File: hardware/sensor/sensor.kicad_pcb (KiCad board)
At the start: 2 copper layers, 29 x 31 mm, 56 parts, among them P1 CONN_01X05, SW1 Reset, T1 BUK9Y22, U1 LMR16006, U2 OPA376AIDCK, U3 CD74HC4046, U4 CD74HC4046, U5 Atmel_SAM_D09, X1 60V, X2 UART

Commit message: Cleanup seems done
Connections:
- P1 pad : (no net) -> GND
- RV1 pad 4: (no net) -> GND
- RV2 pad 4: (no net) -> GND
- U3 pad 14: GND -> Net-(U3-Pad14)
- X2 pad : (no net) -> GND
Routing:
- net GND: track 30.5 -> 41.5 mm, vias 7 -> 9
- net Net-(U5-Pad4): track 15.2 -> 9.69 mm
- net /RX1_out: track 26.4 -> 24.6 mm, vias 3 -> 2

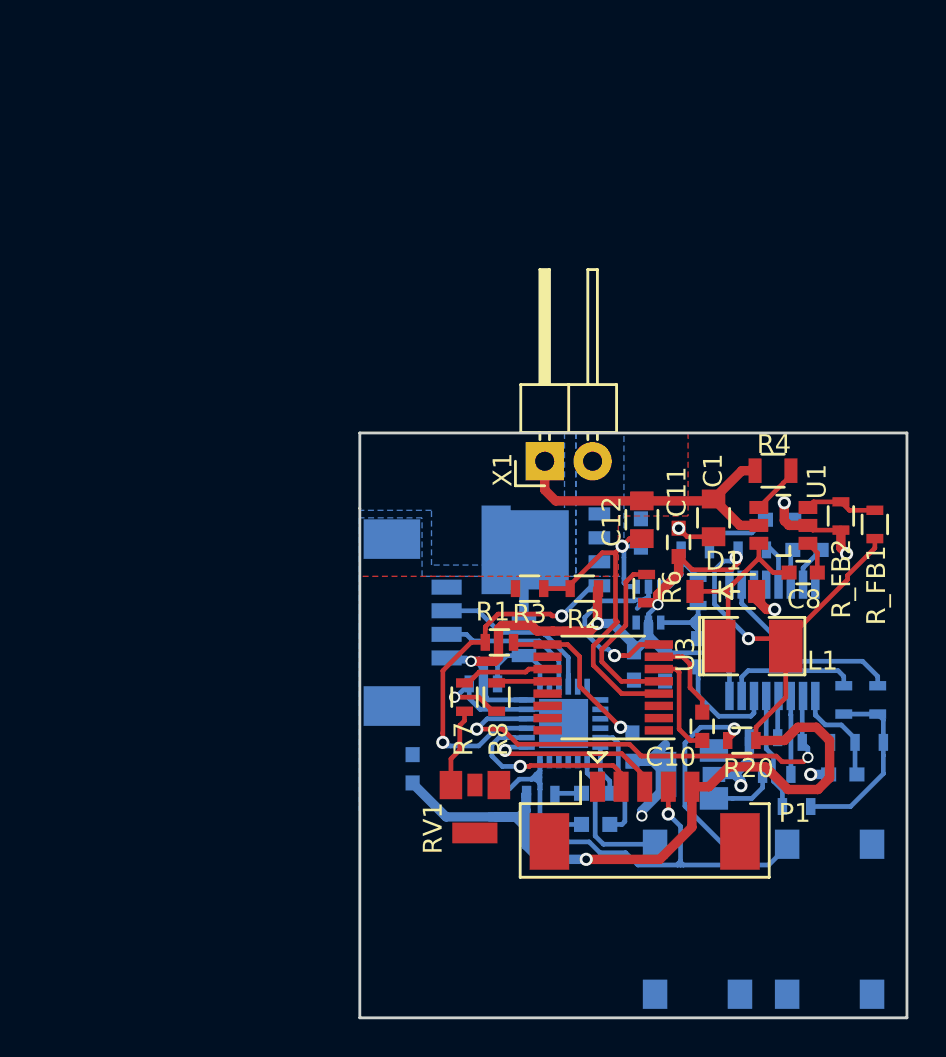
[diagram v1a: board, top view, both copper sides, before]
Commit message: Routing done with Gate Driver. Testpoints are left for now.
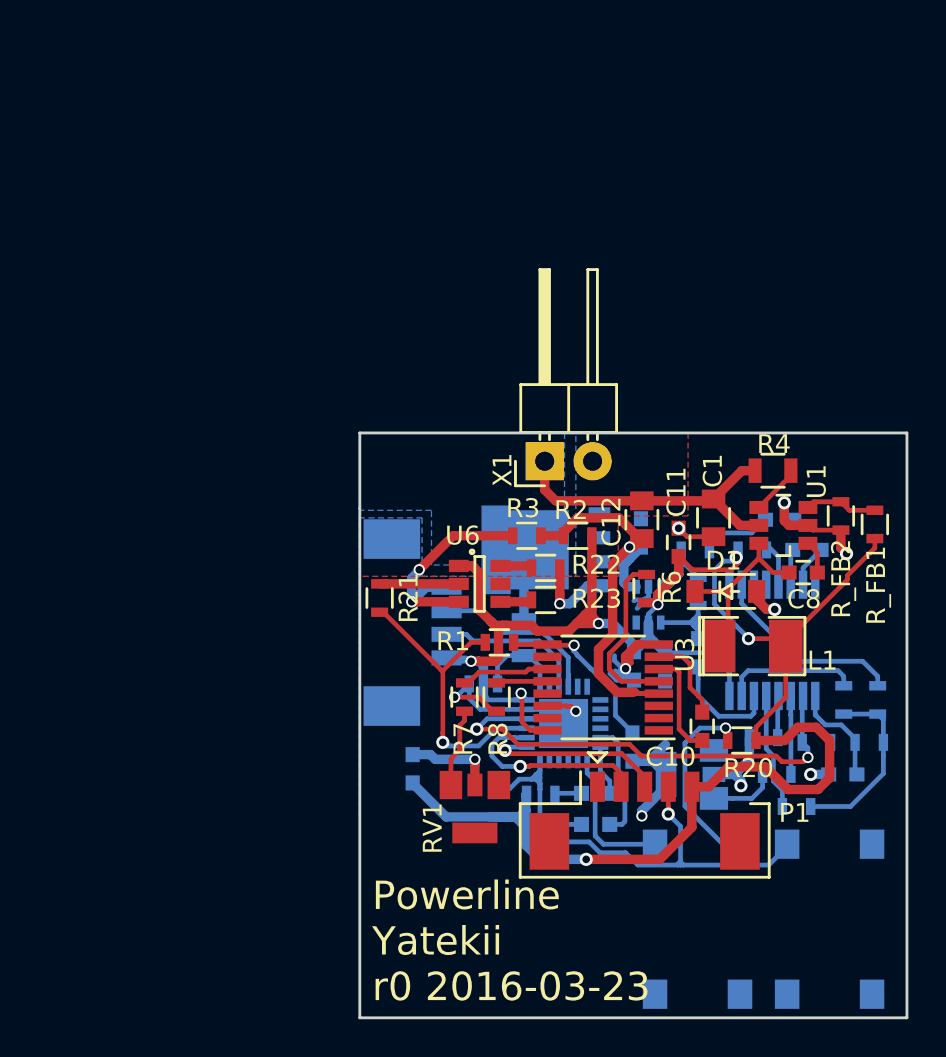
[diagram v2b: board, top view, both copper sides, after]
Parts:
- added R21: 1k, Resistors_SMD:R_0603, F.Cu at (145.1, 83.8)
- added R22: 0R, Resistors_SMD:R_0603, F.Cu at (153.8, 82.2)
- added R23: 0R, Resistors_SMD:R_0603, F.Cu at (153.8, 83.8)
- added U6: ZXGD3005E6_, TO_SOT_Packages_SMD:SOT-23-6, F.Cu at (150.3, 83.0)
- moved R2 2.82 mm to (155.6, 80.5)
- moved R3 2.80 mm to (152.8, 80.5)
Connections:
- RV1 pad 4: GND -> (no net)
- T1 pad 4: /TX1_in -> Net-(R22-Pad2)
- U3 pad 14: Net-(U3-Pad14) -> GND
- U3 pad 16: Net-(U3-Pad16) -> +3V3
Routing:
- net GND: track 41.5 -> 62.4 mm, vias 9 -> 13
- net +3V3: track 102.0 -> 114.5 mm, vias 6 -> 7
- net Net-(R22-Pad2): track 0.00 -> 4.79 mm, vias 0 -> 1
- net Net-(R21-Pad2): track 0.00 -> 4.20 mm
- net /coupling: track 21.2 -> 25.1 mm
- net /TX1_in: track 19.4 -> 16.2 mm, vias 2 -> 1
- net Net-(R23-Pad2): track 0.00 -> 1.69 mm
- net Net-(R22-Pad1): track 0.00 -> 1.69 mm
- net Net-(R20-Pad2): track 11.2 -> 10.6 mm
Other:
- board text added: "Powerline Yatekii r0 2016-03-23"

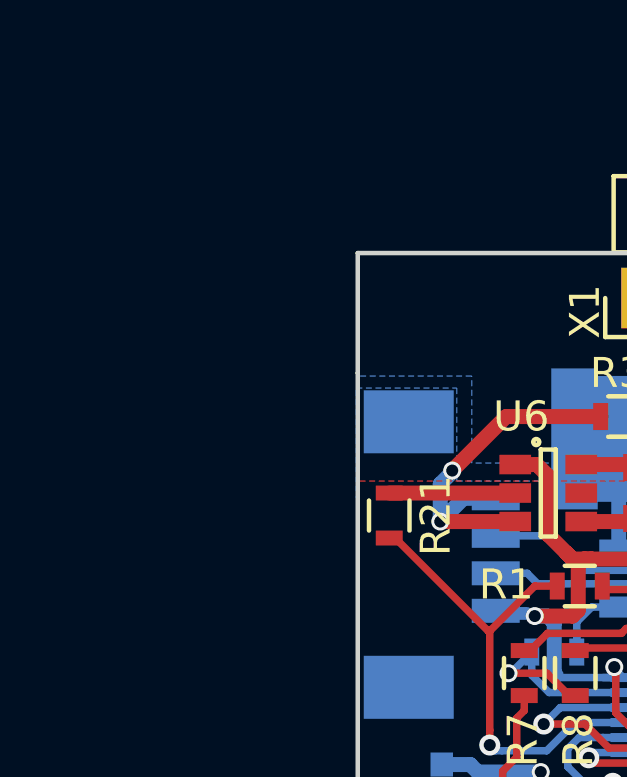
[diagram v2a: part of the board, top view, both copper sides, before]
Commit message: Added footprints; started layouting of the new parts
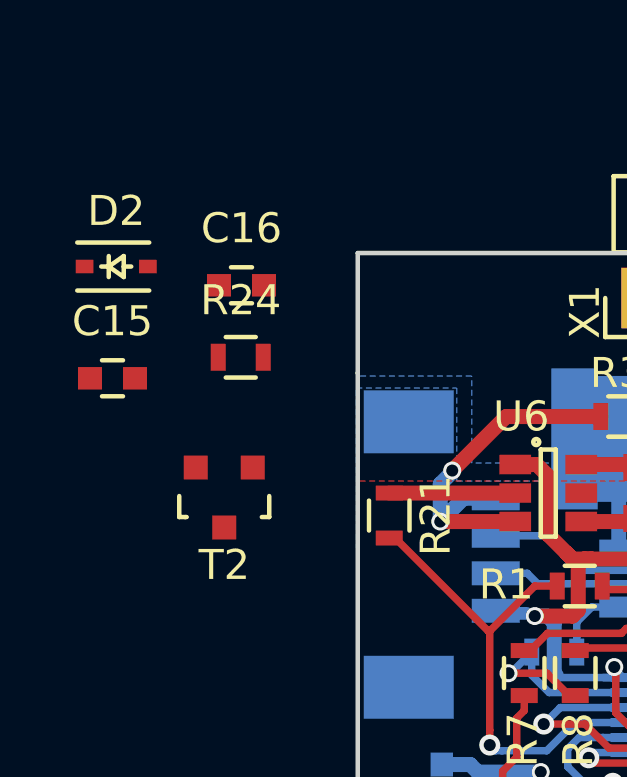
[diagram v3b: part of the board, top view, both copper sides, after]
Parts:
- added C15: C_Small, Capacitors_SMD:C_0603, F.Cu at (135.8, 79.2)
- added C16: C_Small, Capacitors_SMD:C_0603, F.Cu at (140.1, 76.1)
- added D2: ZENER, Diodes_SMD:SOD-323, F.Cu at (135.9, 75.5)
- added R24: R, Resistors_SMD:R_0603, F.Cu at (140.1, 78.5)
- added T2: DMP10H4D2s, TO_SOT_Packages_SMD:SOT-23, F.Cu at (139.6, 83.2)
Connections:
- C1 pad 1: VCC -> Net-(C1-Pad1)
- P1 pad : GND -> (no net)
- R4 pad 1: VCC -> Net-(R4-Pad1)
- RV2 pad 4: GND -> (no net)
- U1 pad 5: VCC -> Net-(C1-Pad1)
- X2 pad : GND -> (no net)
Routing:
- net VCC: track 21.0 -> 15.0 mm
- net Net-(C1-Pad1): track 0.00 -> 5.24 mm
- net Net-(R4-Pad1): track 0.00 -> 0.70 mm

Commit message: Done routing
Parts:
- C16: moved to B.Cu
- moved D2 28.3 mm to (164.2, 76.6), turned to 90 degrees
- moved C16 25.3 mm to (161.4, 89.7), turned to 180 degrees
- moved T2 22.6 mm to (161.2, 76.6), turned to 0 degrees
- moved R24 18.7 mm to (158.7, 76.7), turned to 270 degrees
- moved C15 18.5 mm to (151.2, 89.5), turned to 270 degrees
- moved R7 2.48 mm to (147.1, 88.9)
- moved R8 2.05 mm to (149.3, 89.5)
- moved R4 1.58 mm to (167.4, 76.5)
- moved C1 0.63 mm to (162.7, 80.1)
- moved C12 0.62 mm to (158.5, 80.0)
- moved C9 0.30 mm to (162.2, 86.6)
- moved R1 0.23 mm to (151.4, 85.9)
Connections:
- P1 pad : (no net) -> GND
- R4 pad 1: Net-(R4-Pad1) -> Net-(C1-Pad1)
- RV1 pad 4: (no net) -> GND
- RV2 pad 4: (no net) -> GND
- X2 pad : (no net) -> GND
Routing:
- net Net-(D2-Pad2): track 0.00 -> 7.81 mm, vias 0 -> 2
- net GND: track 62.4 -> 69.8 mm
- net Net-(C1-Pad1): track 5.24 -> 9.28 mm
- net +3V3: track 114.5 -> 117.7 mm
- net Net-(R8-Pad1): track 2.94 -> 5.44 mm
- net Net-(R7-Pad1): track 4.70 -> 7.13 mm
- net /coupling: track 25.1 -> 23.0 mm
- net /SHD: track 2.65 -> 4.44 mm
- net VCC: track 15.0 -> 16.8 mm
- net /TX1_in: track 16.2 -> 17.9 mm, vias 1 -> 2
- net Net-(R4-Pad1): track 0.70 -> 0.00 mm
- net Net-(R7-Pad2): track 4.24 -> 4.78 mm
- net Net-(C9-Pad1): track 5.91 -> 5.56 mm, vias 0 -> 2

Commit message: Added missing 3v3 trace
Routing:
- net +3V3: track 117.7 -> 129.3 mm, vias 7 -> 9
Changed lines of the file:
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@@
   (general
     (links 143)
-    (no_connects 4)
+    (no_connects 3)
     (area 141.225 65.574999 174.375 106.100001)
     (thickness 1.6)
     (drawings 6)
-    (tracks 613)
+    (tracks 623)
     (zones 0)
     (modules 65)
@@
   )
   (setup
-    (last_trace_width 0.25)
+    (last_trace_width 0.5)
     (user_trace_width 0.5)
     (trace_clearance 0.2)
@@
   (segment (start 169.5 80.15) (end 168.00048 80.15) (width 0.25) (layer F.Cu) (net 2))
   (segment (start 168.00048 80.15) (end 167.75048 79.9) (width 0.25) (layer F.Cu) (net 2))
+  (segment (start 147.4 94.2) (end 147.4 94.15) (width 0.5) (layer B.Cu) (net 3))
+  (segment (start 147.4 94.15) (end 146.8 93.55) (width 0.5) (layer B.Cu) (net 3))
+  (via (at 147.4 94.2) (size 0.6) (drill 0.4) (layers F.Cu B.Cu) (net 3))
+  (segment (start 145.6 92.4) (end 147.4 94.2) (width 0.5) (layer F.Cu) (net 3))
+  (segment (start 145.6 87.45) (end 145.6 92.4) (width 0.5) (layer F.Cu) (net 3))
+  (segment (start 147.77501 86.9) (end 146.15 86.9) (width 0.5) (layer F.Cu) (net 3))
+  (segment (start 146.15 86.9) (end 145.6 87.45) (width 0.5) (layer F.Cu) (net 3))
+  (segment (start 148.6 86.925) (end 147.80001 86.925) (width 0.5) (layer B.Cu) (net 3))
+  (segment (start 147.80001 86.925) (end 147.77501 86.9) (width 0.5) (layer B.Cu) (net 3))
+  (via (at 147.77501 86.9) (size 0.6) (drill 0.4) (layers F.Cu B.Cu) (net 3))
   (segment (start 151.967588 89.024994) (end 151.474994 89.024994) (width 0.25) (layer F.Cu) (net 3))
   (segment (start 151.474994 89.024994) (end 151.175 88.725) (width 0.25) (layer F.Cu) (net 3))

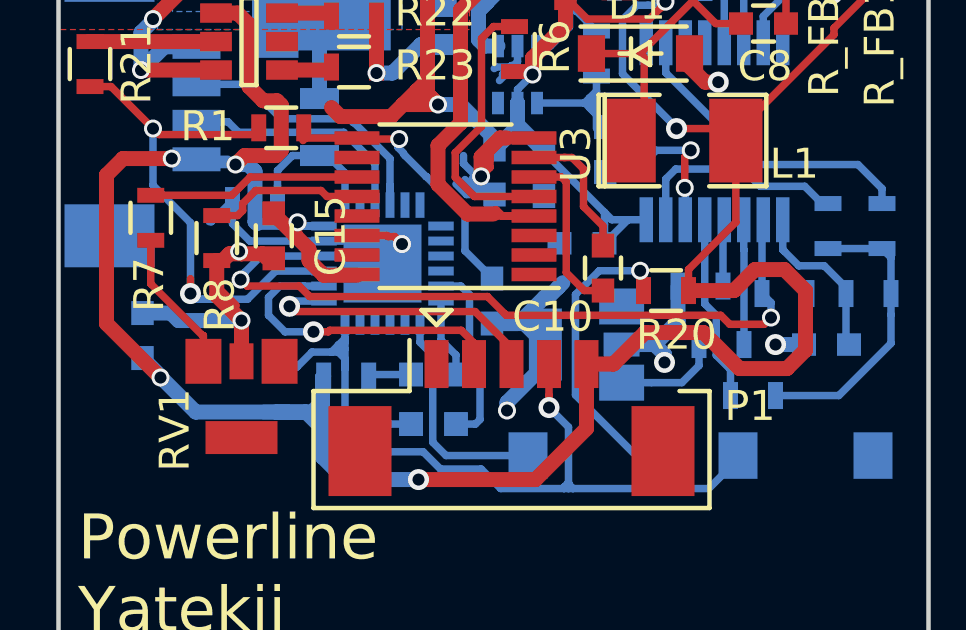
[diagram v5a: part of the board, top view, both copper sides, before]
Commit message: Removed two dead vias and updated gerber files
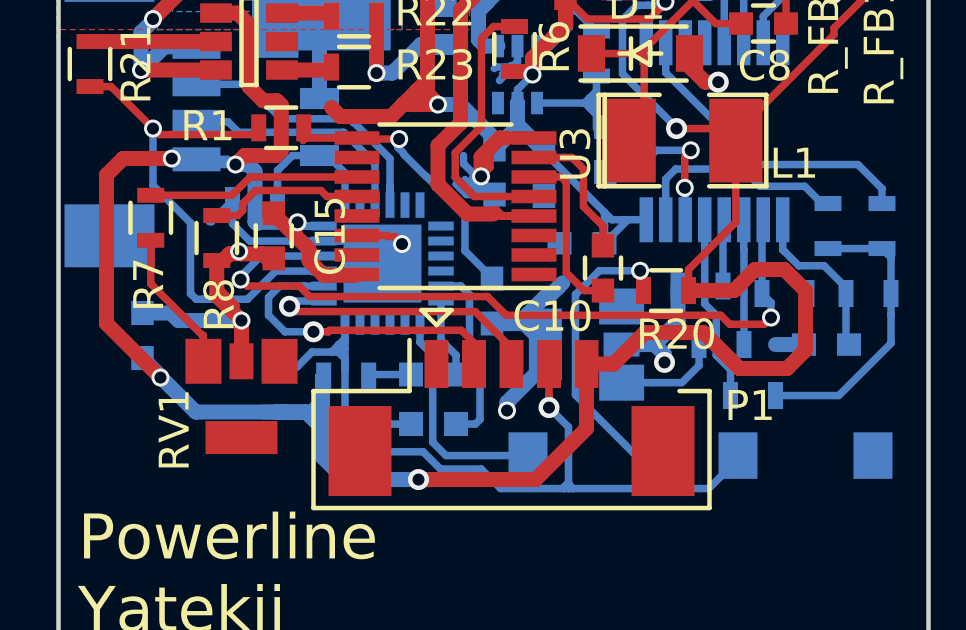
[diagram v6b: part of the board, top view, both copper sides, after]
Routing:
- net /TX1_in: track 17.9 -> 17.4 mm, vias 2 -> 1
- net GND: vias 13 -> 12
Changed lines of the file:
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@@
     (thickness 1.6)
     (drawings 6)
-    (tracks 623)
+    (tracks 620)
     (zones 0)
     (modules 65)
@@
   )
   (setup
-    (last_trace_width 0.5)
+    (last_trace_width 0.25)
     (user_trace_width 0.5)
     (trace_clearance 0.2)
@@
     (visible_elements 7FFFFFFF)
     (pcbplotparams
-      (layerselection 0x00030_80000001)
+      (layerselection 0x0d0f0_80000001)
       (usegerberextensions false)
       (excludeedgelayer true)
@@
       (outputformat 1)
       (mirror false)
-      (drillshape 1)
+      (drillshape 0)
       (scaleselection 1)
-      (outputdirectory ""))
+      (outputdirectory gerber/))
   )
   (net 0 "")
@@
   (segment (start 158.45 92.4) (end 159.325 92.4) (width 0.5) (layer B.Cu) (net 2))
   (segment (start 168.85 93.1) (end 167.9 93.1) (width 0.5) (layer B.Cu) (net 2))
-  (via (at 167.9 93.1) (size 0.7) (drill 0.4) (layers F.Cu B.Cu) (net 2))
   (segment (start 164.2 93.43) (end 164.2 93.69499) (width 0.5) (layer B.Cu) (net 2))
   (via (at 164.2 93.69499) (size 0.7) (drill 0.4) (layers F.Cu B.Cu) (net 2))
@@
   (segment (start 145.75 84.5) (end 145.05 84.5) (width 0.25) (layer F.Cu) (net 17))
   (segment (start 145.05 84.5) (end 145.25 84.5) (width 0.25) (layer F.Cu) (net 17))
-  (segment (start 148.4 90.905026) (end 148.4 91.4) (width 0.25) (layer F.Cu) (net 17))
-  (via (at 148.4 91.4) (size 0.7) (drill 0.4) (layers F.Cu B.Cu) (net 17))
   (segment (start 148.589578 91.589578) (end 148.4 91.4) (width 0.25) (layer B.Cu) (net 17))
   (segment (start 148.810422 91.589578) (end 148.589578 91.589578) (width 0.25) (layer B.Cu) (net 17))

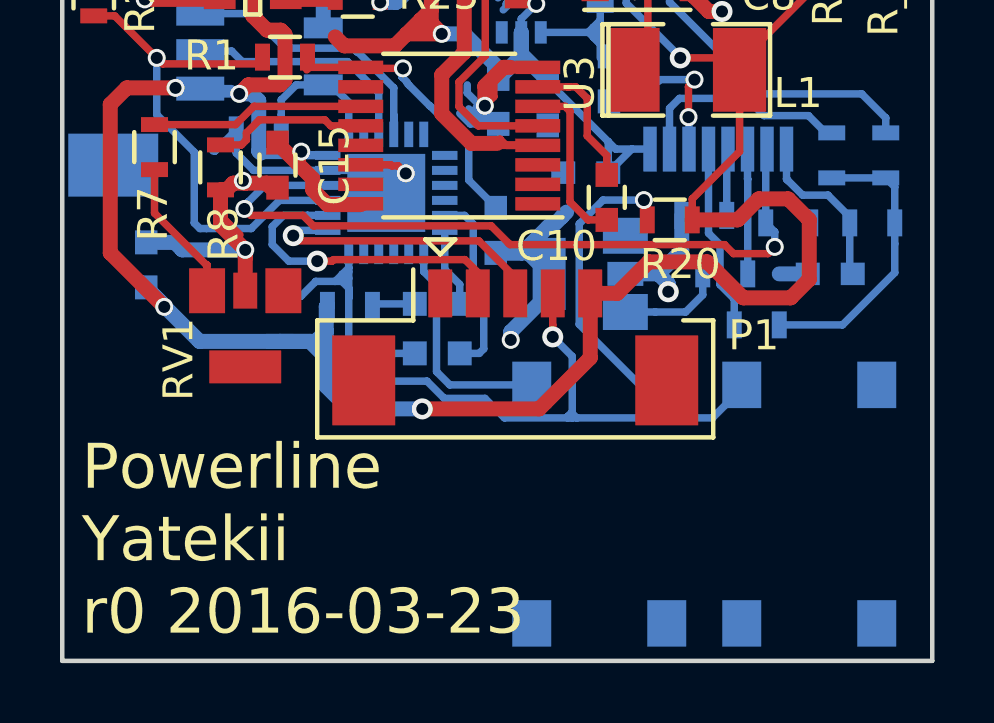
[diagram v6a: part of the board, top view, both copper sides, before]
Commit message: Fixed push button and added debouncing
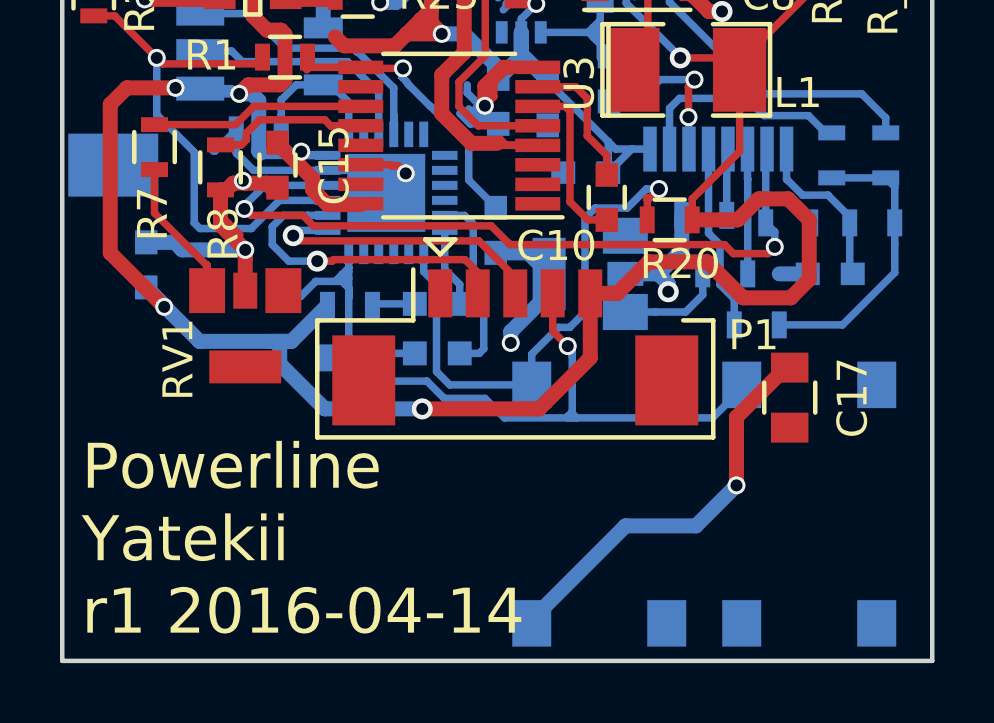
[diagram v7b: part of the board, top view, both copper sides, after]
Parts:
- added C17: 1u, Capacitors_SMD:C_0805, F.Cu at (168.2, 97.2)
- C15, C16: value C_Small -> 100n
- R24: value R -> 100k
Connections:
- R18 pad 1: +3V3 -> Net-(R18-Pad1)
- R20 pad 2: Net-(R20-Pad2) -> /SW_CSTM
- SW_CSTM1 pad 2: Net-(R20-Pad2) -> GND
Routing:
- net /SW_CSTM: track 7.54 -> 32.1 mm, vias 0 -> 2
- net Net-(R20-Pad2): track 10.6 -> 0.00 mm, vias 1 -> 0
- net GND: track 69.8 -> 67.8 mm
- net +3V3: track 129.3 -> 127.9 mm
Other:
- board text added: "Powerline Yatekii r1 2016-04-14"
- board text removed: "Powerline Yatekii r0 2016-03-23"

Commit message: PCB and schematic V2
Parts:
- removed R22, R23: 0R, Resistors_SMD:R_0603
- removed T1: BUK9Y22, TO_SOT_Packages_SMD:SOT-669_LFPAK
- removed U6: ZXGD3005E6_, TO_SOT_Packages_SMD:SOT-23-6
- added C18: C_Small, Capacitors_SMD:C_0603, B.Cu at (134.6, 81.8)
- added JP3.4: R_Small, Resistors_SMD:R_0603, B.Cu at (129.5, 92.7)
- C1: footprint Capacitors_SMD:C_0805 -> Capacitors_SMD:C_1210
- C11: footprint Capacitors_SMD:C_0603 -> Capacitors_SMD:C_1206
- C12, C17, D1, R2, R3, X1: moved to B.Cu
- C3, R15, SW1, SW_CSTM1: moved to F.Cu
- D_BLUE1, D_RED1: footprint LEDs:LED-0603 -> LEDs:LED_0603
- P1: footprint Connectors_Molex:Connector_Molex_PicoBlade_53261-0571 -> Connectors_Molex:Molex_PicoBlade_53261-0571
- R1: value R_Small -> 10k
- R21: value 1k -> 100k
- U3, U4: footprint Housings_SSOP:TSSOP-16_4.4x5mm_Pitch0.65mm -> Housings_SOIC:SOIC-16_7.5x10.3mm_Pitch1.27mm
- X2: footprint Connectors_Molex:Connector_Molex_PicoBlade_53261-0471 -> Connectors_Molex:Molex_PicoBlade_53261-0471
- moved SW1 45.3 mm to (132.5, 73.9), turned to 0 degrees
- moved D1 42.1 mm to (128.5, 59.8), turned to 90 degrees
- moved JP3.1 42.0 mm to (129.8, 94.5), turned to 180 degrees
- moved L1 40.5 mm to (129.0, 67.3), turned to 270 degrees
- moved R_FB1 40.4 mm to (132.3, 69.1), turned to 0 degrees
- moved C8 39.4 mm to (131.6, 66.3), turned to 90 degrees
- moved RV1 38.4 mm to (141.0, 57.7), turned to 0 degrees
- moved C13 37.9 mm to (130.6, 88.9), turned to 90 degrees
- moved R11 36.6 mm to (129.5, 90.9), turned to 0 degrees
- moved R_FB2 36.1 mm to (134.9, 69.1), turned to 0 degrees
- moved SW_CSTM1 35.5 mm to (132.6, 80.8), turned to 0 degrees
- moved U1 35.5 mm to (133.7, 66.3), turned to 0 degrees
- moved C3 34.8 mm to (147.3, 58.7), turned to 180 degrees
- moved C1 34.5 mm to (134.6, 60.1), turned to 90 degrees
- moved R24 34.3 mm to (128.8, 59.9), turned to 180 degrees
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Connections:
- R11 pad 1: Net-(R11-Pad1) -> GND
- R11 pad 2: +3V3 -> Net-(R11-Pad2)
- R12 pad 2: Net-(R12-Pad2) -> GND
- R13 pad 2: GND -> Net-(R13-Pad2)
- R18 pad 1: Net-(R18-Pad1) -> +3V3
- R21 pad 1: /TX1_in -> +3V3
- R21 pad 2: Net-(R21-Pad2) -> Net-(C3-Pad1)
- R6 pad 1: +3V3 -> GND
- R7 pad 2: Net-(R7-Pad2) -> GND
- R8 pad 2: GND -> Net-(R8-Pad2)
- RV1 pad 3: Net-(R7-Pad2) -> Net-(R8-Pad2)
- RV1 pad 4: GND -> (no net)
- RV2 pad 1: Net-(RV2-Pad1) -> Net-(R13-Pad2)
- RV2 pad 3: Net-(R12-Pad2) -> Net-(RV2-Pad3)
- RV2 pad 4: GND -> (no net)
- U3 pad 3: Net-(U3-Pad3) -> GND
- U4 pad 4: /JP2 -> Net-(JP3.4-Pad1)
- U4 pad 5: Net-(R11-Pad1) -> Net-(R11-Pad2)
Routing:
- net VCC: track 16.8 -> 62.5 mm, vias 0 -> 2
- net GND: track 67.8 -> 101.4 mm, vias 12 -> 10
- net /coupling: track 23.0 -> 55.8 mm, vias 1 -> 2
- net Net-(P1-Pad4): track 27.6 -> 58.6 mm
- net +3V3: track 127.9 -> 157.8 mm
- net /VCOin: track 9.73 -> 34.5 mm
- net /TX1_in: track 17.4 -> 38.9 mm
- net /RX1_out: track 25.0 -> 13.2 mm, vias 2 -> 0
- net Net-(JP3.1-Pad1): track 10.3 -> 1.50 mm
- net Net-(R6-Pad2): track 9.14 -> 1.50 mm
- net /SW_CSTM: track 32.1 -> 24.5 mm, vias 2 -> 1
- net Net-(P1-Pad3): track 10.3 -> 16.7 mm
- net Net-(P1-Pad2): track 10.7 -> 15.8 mm
- net Net-(R22-Pad2): track 4.79 -> 0.00 mm, vias 1 -> 0
- net Net-(R7-Pad2): track 4.78 -> 0.00 mm
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- removed copper zone on B.Cu, net VCC
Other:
- board size 29 x 31 mm -> 25.7 x 45.5 mm
- net class pro4_default removed
- rule pad_to_mask_clearance: 0.2 -> 0
- rule trace_min: 0.2 -> 0.24
- rule via_min_size: 0.4 -> 0.9
- board text removed: "Powerline Yatekii r1 2016-04-14"
